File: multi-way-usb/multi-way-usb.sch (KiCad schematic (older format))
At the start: 60 parts, among them J1 USB_A, J10 USB_A, J11 USB_A, J12 USB_A, J13 USB_A, J14 USB_A, J15 USB_A, J16 USB_A, J17 USB_A, J18 USB_A, J19 USB_A, J2 USB_A, J20 USB_A, J21 USB_A, J22 USB_A, J23 USB_A, J24 USB_A, J25 USB_B_Micro, J26 USB_B_Micro, J27 Conn_01x02, J28 Conn_01x02, J3 USB_A, J4 USB_A, J5 USB_A, J6 USB_A, J7 USB_A, J8 USB_A, J9 USB_A

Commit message: multi-way-usb: Changed footprint for inverted connectors
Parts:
- J1, J10, J11, J12, J13, J14, J15, J2, J3, J4, J5, J6, J7, J8, J9: footprint tom-connectors:OST_USB-A1HSW6 -> tom-connectors:OST_USB-A1HSW6-INVERTED
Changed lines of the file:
@@
 F 0 "J1" H 3407 1717 50  0000 C CNN
 F 1 "USB_A" H 3407 1626 50  0000 C CNN
-F 2 "tom-connectors:OST_USB-A1HSW6" H 3500 1200 50  0001 C CNN
+F 2 "tom-connectors:OST_USB-A1HSW6-INVERTED" H 3500 1200 50  0001 C CNN
 F 3 " ~" H 3500 1200 50  0001 C CNN
 F 4 "C42642" H 3350 1250 50  0001 C CNN "LCSC"
@@
 F 0 "J7" H 3407 2867 50  0000 C CNN
 F 1 "USB_A" H 3407 2776 50  0000 C CNN
-F 2 "tom-connectors:OST_USB-A1HSW6" H 3500 2350 50  0001 C CNN
+F 2 "tom-connectors:OST_USB-A1HSW6-INVERTED" H 3500 2350 50  0001 C CNN
 F 3 " ~" H 3500 2350 50  0001 C CNN
 F 4 "C42642" H 3350 2400 50  0001 C CNN "LCSC"
@@
 F 0 "J3" H 6207 1717 50  0000 C CNN
 F 1 "USB_A" H 6207 1626 50  0000 C CNN
-F 2 "tom-connectors:OST_USB-A1HSW6" H 6300 1200 50  0001 C CNN
+F 2 "tom-connectors:OST_USB-A1HSW6-INVERTED" H 6300 1200 50  0001 C CNN
 F 3 " ~" H 6300 1200 50  0001 C CNN
 F 4 "C42642" H 6150 1250 50  0001 C CNN "LCSC"
@@
 F 0 "J9" H 6207 2867 50  0000 C CNN
 F 1 "USB_A" H 6207 2776 50  0000 C CNN
-F 2 "tom-connectors:OST_USB-A1HSW6" H 6300 2350 50  0001 C CNN
+F 2 "tom-connectors:OST_USB-A1HSW6-INVERTED" H 6300 2350 50  0001 C CNN
 F 3 " ~" H 6300 2350 50  0001 C CNN
 F 4 "C42642" H 6150 2400 50  0001 C CNN "LCSC"
@@
 F 0 "J2" H 4657 1717 50  0000 C CNN
 F 1 "USB_A" H 4657 1626 50  0000 C CNN
-F 2 "tom-connectors:OST_USB-A1HSW6" H 4750 1200 50  0001 C CNN
+F 2 "tom-connectors:OST_USB-A1HSW6-INVERTED" H 4750 1200 50  0001 C CNN
 F 3 " ~" H 4750 1200 50  0001 C CNN
 F 4 "C42642" H 4600 1250 50  0001 C CNN "LCSC"
@@
 F 0 "J8" H 4657 2867 50  0000 C CNN
 F 1 "USB_A" H 4657 2776 50  0000 C CNN
-F 2 "tom-connectors:OST_USB-A1HSW6" H 4750 2350 50  0001 C CNN
+F 2 "tom-connectors:OST_USB-A1HSW6-INVERTED" H 4750 2350 50  0001 C CNN
 F 3 " ~" H 4750 2350 50  0001 C CNN
 F 4 "C42642" H 4600 2400 50  0001 C CNN "LCSC"
@@
 F 0 "J4" H 7457 1717 50  0000 C CNN
 F 1 "USB_A" H 7457 1626 50  0000 C CNN
-F 2 "tom-connectors:OST_USB-A1HSW6" H 7550 1200 50  0001 C CNN
+F 2 "tom-connectors:OST_USB-A1HSW6-INVERTED" H 7550 1200 50  0001 C CNN
 F 3 " ~" H 7550 1200 50  0001 C CNN
 F 4 "C42642" H 7400 1250 50  0001 C CNN "LCSC"
@@
 F 0 "J10" H 7457 2867 50  0000 C CNN
 F 1 "USB_A" H 7457 2776 50  0000 C CNN
-F 2 "tom-connectors:OST_USB-A1HSW6" H 7550 2350 50  0001 C CNN
+F 2 "tom-connectors:OST_USB-A1HSW6-INVERTED" H 7550 2350 50  0001 C CNN
 F 3 " ~" H 7550 2350 50  0001 C CNN
 F 4 "C42642" H 7400 2400 50  0001 C CNN "LCSC"
@@
 F 0 "J5" H 9007 1717 50  0000 C CNN
 F 1 "USB_A" H 9007 1626 50  0000 C CNN
-F 2 "tom-connectors:OST_USB-A1HSW6" H 9100 1200 50  0001 C CNN
+F 2 "tom-connectors:OST_USB-A1HSW6-INVERTED" H 9100 1200 50  0001 C CNN
 F 3 " ~" H 9100 1200 50  0001 C CNN
 F 4 "C42642" H 8950 1250 50  0001 C CNN "LCSC"
@@
 F 0 "J11" H 9007 2867 50  0000 C CNN
 F 1 "USB_A" H 9007 2776 50  0000 C CNN
-F 2 "tom-connectors:OST_USB-A1HSW6" H 9100 2350 50  0001 C CNN
+F 2 "tom-connectors:OST_USB-A1HSW6-INVERTED" H 9100 2350 50  0001 C CNN
 F 3 " ~" H 9100 2350 50  0001 C CNN
 F 4 "C42642" H 8950 2400 50  0001 C CNN "LCSC"
@@
 F 0 "J6" H 10257 1717 50  0000 C CNN
 F 1 "USB_A" H 10257 1626 50  0000 C CNN
-F 2 "tom-connectors:OST_USB-A1HSW6" H 10350 1200 50  0001 C CNN
+F 2 "tom-connectors:OST_USB-A1HSW6-INVERTED" H 10350 1200 50  0001 C CNN
 F 3 " ~" H 10350 1200 50  0001 C CNN
 F 4 "C42642" H 10200 1250 50  0001 C CNN "LCSC"
@@
 F 0 "J12" H 10257 2867 50  0000 C CNN
 F 1 "USB_A" H 10257 2776 50  0000 C CNN
-F 2 "tom-connectors:OST_USB-A1HSW6" H 10350 2350 50  0001 C CNN
+F 2 "tom-connectors:OST_USB-A1HSW6-INVERTED" H 10350 2350 50  0001 C CNN
 F 3 " ~" H 10350 2350 50  0001 C CNN
 F 4 "C42642" H 10200 2400 50  0001 C CNN "LCSC"
@@
 F 0 "J13" H 3407 4167 50  0000 C CNN
 F 1 "USB_A" H 3407 4076 50  0000 C CNN
-F 2 "tom-connectors:OST_USB-A1HSW6" H 3500 3650 50  0001 C CNN
+F 2 "tom-connectors:OST_USB-A1HSW6-INVERTED" H 3500 3650 50  0001 C CNN
 F 3 " ~" H 3500 3650 50  0001 C CNN
 F 4 "C42642" H 3350 3700 50  0001 C CNN "LCSC"
@@
 F 0 "J14" H 4657 4167 50  0000 C CNN
 F 1 "USB_A" H 4657 4076 50  0000 C CNN
-F 2 "tom-connectors:OST_USB-A1HSW6" H 4750 3650 50  0001 C CNN
+F 2 "tom-connectors:OST_USB-A1HSW6-INVERTED" H 4750 3650 50  0001 C CNN
 F 3 " ~" H 4750 3650 50  0001 C CNN
 F 4 "C42642" H 4600 3700 50  0001 C CNN "LCSC"
@@
 F 0 "J15" H 6207 4167 50  0000 C CNN
 F 1 "USB_A" H 6207 4076 50  0000 C CNN
-F 2 "tom-connectors:OST_USB-A1HSW6" H 6300 3650 50  0001 C CNN
+F 2 "tom-connectors:OST_USB-A1HSW6-INVERTED" H 6300 3650 50  0001 C CNN
 F 3 " ~" H 6300 3650 50  0001 C CNN
 F 4 "C42642" H 6150 3700 50  0001 C CNN "LCSC"

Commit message: multi-way-usb: fix mechanical issues
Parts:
- added F15, F16: 100mA/250mA, tom-passives:C_1206_3216Metric, symbol tom-passives:FUSE
- added J15, J16: USB_A, tom-connectors:CUI_UJ2-AV-1-TH, symbol tom-connectors:USB_A
- J17: renamed from J14; footprint tom-connectors:OST_USB-A1HSW6-INVERTED -> tom-connectors:CUI_UJ2-AV-1-TH
- J7: renamed from J3; footprint tom-connectors:OST_USB-A1HSW6-INVERTED -> tom-connectors:CUI_UJ2-AV-1-TH
- J8: renamed from J6; footprint tom-connectors:OST_USB-A1HSW6-INVERTED -> tom-connectors:CUI_UJ2-AV-1-TH
- J9: renamed from J10; footprint tom-connectors:OST_USB-A1HSW6-INVERTED -> tom-connectors:CUI_UJ2-AV-1-TH
- renumbered D2 to D1, D1 to D2, F9 to F10, F15 to F14, F14 to F17, F17 to F19, F16 to F20, F20 to F22, F19 to F23, F23 to F25, F22 to F26, F4 to F3, F5 to F4, F7 to F5, F8 to F6, F3 to F7, F6 to F8, F10 to F9, J9 to J10, J15 to J14, J17 to J19, J16 to J20, J20 to J22, J19 to J23, J23 to J25, J22 to J26, J4 to J3, J5 to J4, J7 to J5, J8 to J6, R2 to R1, R1 to R2, J25 to X1, J26 to X2, J27 to X3, J28 to X4
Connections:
- net +5VA: now also F15.2, F16.2
- net GND: now also J15.4 (GND), J15.5 (Shield), J16.4 (GND), J16.5 (Shield)
- new net: F16.1, J16.1 (VBUS)
- new net: F15.1, J15.1 (VBUS)
- no-connect marks 54 -> 58
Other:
- moved on the sheet: F10, F11, F12, F13, F14, F17, F18, F19, F20, F21, F22, F23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

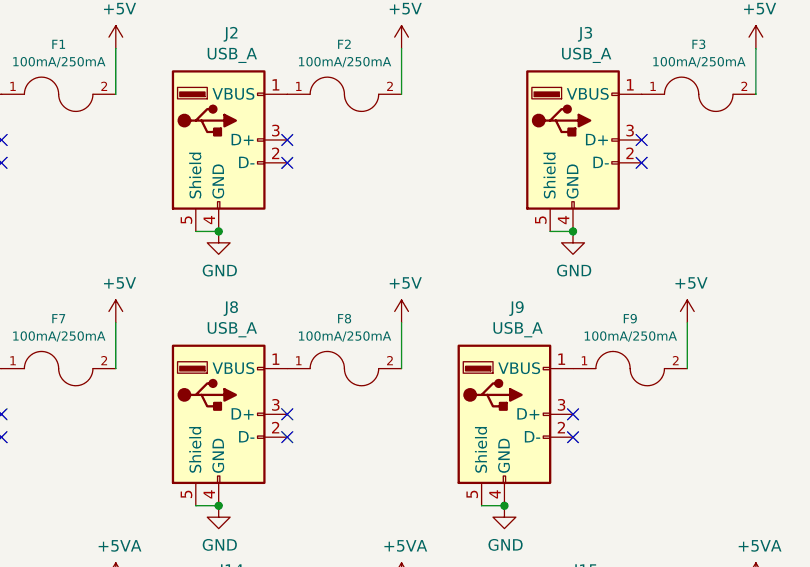
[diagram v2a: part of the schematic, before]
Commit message: multi-way-usb: move J8 to X2 to balance supplies, v1.2 ready for production
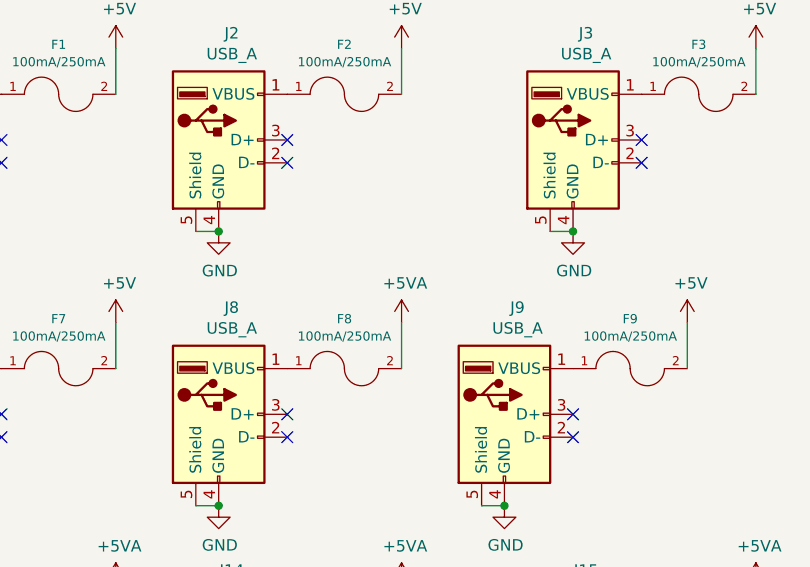
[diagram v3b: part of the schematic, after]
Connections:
- net +5V: no longer F8.2
- net +5VA: now also F8.2
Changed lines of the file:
@@
-	1    0    0    -1
-$EndComp
-$Comp
-L power:+5V #PWR019
-U 1 1 5F64DF1E
-P 6650 2050
-F 0 "#PWR019" H 6650 1900 50  0001 C CNN
-F 1 "+5V" H 6665 2223 50  0000 C CNN
-F 2 "" H 6650 2050 50  0001 C CNN
-F 3 "" H 6650 2050 50  0001 C CNN
-	1    6650 2050
 	1    0    0    -1
 $EndComp
@@
 F 4 "C20981" H 5150 2250 50  0001 C CNN "LCSC"
 	1    5150 2250
-	1    0    0    -1
-$EndComp
-$Comp
-L power:+5V #PWR018
-U 1 1 5F6B45C5
-P 5400 2050
-F 0 "#PWR018" H 5400 1900 50  0001 C CNN
-F 1 "+5V" H 5415 2223 50  0000 C CNN
-F 2 "" H 5400 2050 50  0001 C CNN
-F 3 "" H 5400 2050 50  0001 C CNN
-	1    5400 2050
 	1    0    0    -1
 $EndComp
@@
 	1    0    0    -1
 $EndComp
+$Comp
+L power:+5V #PWR019
+U 1 1 5F64DF1E
+P 6650 2050
+F 0 "#PWR019" H 6650 1900 50  0001 C CNN
+F 1 "+5V" H 6665 2223 50  0000 C CNN
+F 2 "" H 6650 2050 50  0001 C CNN
+F 3 "" H 6650 2050 50  0001 C CNN
+	1    6650 2050
+	1    0    0    -1
+$EndComp
+$Comp
+L power:+5VA #PWR?
+U 1 1 5FEBC637
+P 5400 2050
+F 0 "#PWR?" H 5400 1900 50  0001 C CNN
+F 1 "+5VA" H 5415 2223 50  0000 C CNN
+F 2 "" H 5400 2050 50  0001 C CNN
+F 3 "" H 5400 2050 50  0001 C CNN
+	1    5400 2050
+	1    0    0    -1
+$EndComp
